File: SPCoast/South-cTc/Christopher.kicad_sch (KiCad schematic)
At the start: 23 parts, among them U28 0x27, U29 0x28, U30 0x29

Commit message: SPCoast: owner's edits: schematics synced with the revised symbol libraries (baseline)
Update Symbols from Library on all plant and desk sheets; CP values for
Christopher, GilroyInterchange and Luchessa; Restricted Speed markers
consolidated in Corporal, Luchessa and Sargent.

Observed in the diff, not changed by the sweep that follows: CP changed on 23
symbols (Christopher: prefix removed, 815/815A/IND now Christopher North) and
added on 12 (GilroyInterchange); two lamps' Color reset to their symbol variant
(Christopher LMP93 red -> yellow, Sargent LMP133 yellow -> red).

Verified: netlists keep their net counts (Christopher 33, Corporal 26,
GilroyCalTrain 27, GilroyInterchange 22, Luchessa 34, Sargent 18, Watsonville
96, South-cTc 341); desk compiles to 75 appliances, 137 bindings, 14 columns;
no root-UUID regression.

Co-Authored-By: Claude Sonnet 5.5 <noreply@anthropic.com>
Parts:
- LMP93: Color red -> yellow
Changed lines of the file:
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@@
 			)
 		)
-		(property "Description" "One physical desk lamp. Value is a free descriptive label (e.g. OS, TRACK, MC) and is not used elsewhere. IndicationToken is a comma-separated list of indication names (track circuits such as 795T1,2NAA,799T1, or tokens such as MC1K) OR'd to drive this one lamp. All listed indications are still individually on the CodeLine wire"
+		(property "Description" "One physical model board lamp. Value is a free descriptive label (e.g. OS, TRACK, MC) and is not used elsewhere. IndicationToken is a comma-separated list of indication names (track circuits such as 795T1,2NAA,799T1, or tokens such as MC1K) OR'd to drive this one lamp. All listed indications are still individually on the CodeLine wire"
 			(at 181.61 111.76 0)
 			(hide yes)
@@
 			)
 		)
-		(property "Description" "One physical desk lamp. Value is a free descriptive label (e.g. OS, TRACK, MC) and is not used elsewhere. IndicationToken is a comma-separated list of indication names (track circuits such as 795T1,2NAA,799T1, or tokens such as MC1K) OR'd to drive this one lamp. All listed indications are still individually on the CodeLine wire"
+		(property "Description" "One physical model board lamp. Value is a free descriptive label (e.g. OS, TRACK, MC) and is not used elsewhere. IndicationToken is a comma-separated list of indication names (track circuits such as 795T1,2NAA,799T1, or tokens such as MC1K) OR'd to drive this one lamp. All listed indications are still individually on the CodeLine wire"
 			(at 130.175 36.195 0)
 			(hide yes)
@@
 			)
 		)
-		(property "Description" "One physical desk lamp. Value is a free descriptive label (e.g. OS, TRACK, MC) and is not used elsewhere. IndicationToken is a comma-separated list of indication names (track circuits such as 795T1,2NAA,799T1, or tokens such as MC1K) OR'd to drive this one lamp. All listed indications are still individually on the CodeLine wire"
+		(property "Description" "One physical model board lamp. Value is a free descriptive label (e.g. OS, TRACK, MC) and is not used elsewhere. IndicationToken is a comma-separated list of indication names (track circuits such as 795T1,2NAA,799T1, or tokens such as MC1K) OR'd to drive this one lamp. All listed indications are still individually on the CodeLine wire"
 			(at 181.61 39.37 0)
 			(hide yes)
@@
 			)
 		)
-		(property "Description" "One physical desk lamp. Value is a free descriptive label (e.g. OS, TRACK, MC) and is not used elsewhere. IndicationToken is a comma-separated list of indication names (track circuits such as 795T1,2NAA,799T1, or tokens such as MC1K) OR'd to drive this one lamp. All listed indications are still individually on the CodeLine wire"
+		(property "Description" "One physical model board lamp. Value is a free descriptive label (e.g. OS, TRACK, MC) and is not used elsewhere. IndicationToken is a comma-separated list of indication names (track circuits such as 795T1,2NAA,799T1, or tokens such as MC1K) OR'd to drive this one lamp. All listed indications are still individually on the CodeLine wire"
 			(at 80.01 44.45 0)
 			(hide yes)
@@
 			)
 		)
-		(property "Description" "One physical desk lamp. Value is a free descriptive label (e.g. OS, TRACK, MC) and is not used elsewhere. IndicationToken is a comma-separated list of indication names (track circuits such as 795T1,2NAA,799T1, or tokens such as MC1K) OR'd to drive this one lamp. All listed indications are still individually on the CodeLine wire"
+		(property "Description" "One physical model board lamp. Value is a free descriptive label (e.g. OS, TRACK, MC) and is not used elsewhere. IndicationToken is a comma-separated list of indication names (track circuits such as 795T1,2NAA,799T1, or tokens such as MC1K) OR'd to drive this one lamp. All listed indications are still individually on the CodeLine wire"
 			(at 181.61 44.45 0)
 			(hide yes)
@@
 			)
 		)
-		(property "Color" "red"
+		(property "Color" "yellow"
 			(at 181.61 43.18 0)
 			(hide yes)
@@
 			)
 		)
-		(property "Description" "One physical desk lamp. Value is a free descriptive label (e.g. OS, TRACK, MC) and is not used elsewhere. IndicationToken is a comma-separated list of indication names (track circuits such as 795T1,2NAA,799T1, or tokens such as MC1K) OR'd to drive this one lamp. All listed indications are still individually on the CodeLine wire"
+		(property "Description" "One physical model board lamp. Value is a free descriptive label (e.g. OS, TRACK, MC) and is not used elsewhere. IndicationToken is a comma-separated list of indication names (track circuits such as 795T1,2NAA,799T1, or tokens such as MC1K) OR'd to drive this one lamp. All listed indications are still individually on the CodeLine wire"
 			(at 80.01 39.37 0)
 			(hide yes)
@@
 			)
 		)
-		(property "Description" "One physical desk lamp. Value is a free descriptive label (e.g. OS, TRACK, MC) and is not used elsewhere. IndicationToken is a comma-separated list of indication names (track circuits such as 795T1,2NAA,799T1, or tokens such as MC1K) OR'd to drive this one lamp. All listed indications are still individually on the CodeLine wire"
+		(property "Description" "One physical model board lamp. Value is a free descriptive label (e.g. OS, TRACK, MC) and is not used elsewhere. IndicationToken is a comma-separated list of indication names (track circuits such as 795T1,2NAA,799T1, or tokens such as MC1K) OR'd to drive this one lamp. All listed indications are still individually on the CodeLine wire"
 			(at 80.01 34.29 0)
 			(hide yes)
@@
 			)
 		)
-		(property "Description" "One physical desk lamp. Value is a free descriptive label (e.g. OS, TRACK, MC) and is not used elsewhere. IndicationToken is a comma-separated list of indication names (track circuits such as 795T1,2NAA,799T1, or tokens such as MC1K) OR'd to drive this one lamp. All listed indications are still individually on the CodeLine wire"
+		(property "Description" "One physical model board lamp. Value is a free descriptive label (e.g. OS, TRACK, MC) and is not used elsewhere. IndicationToken is a comma-separated list of indication names (track circuits such as 795T1,2NAA,799T1, or tokens such as MC1K) OR'd to drive this one lamp. All listed indications are still individually on the CodeLine wire"
 			(at 80.01 111.76 0)
 			(hide yes)
@@
 			)
 		)
-		(property "Description" "One physical desk lamp. Value is a free descriptive label (e.g. OS, TRACK, MC) and is not used elsewhere. IndicationToken is a comma-separated list of indication names (track circuits such as 795T1,2NAA,799T1, or tokens such as MC1K) OR'd to drive this one lamp. All listed indications are still individually on the CodeLine wire"
+		(property "Description" "One physical model board lamp. Value is a free descriptive label (e.g. OS, TRACK, MC) and is not used elsewhere. IndicationToken is a comma-separated list of indication names (track circuits such as 795T1,2NAA,799T1, or tokens such as MC1K) OR'd to drive this one lamp. All listed indications are still individually on the CodeLine wire"
 			(at 130.175 41.275 0)
 			(hide yes)
@@
 			)
 		)
-		(property "Description" "Generic 1-bit dispatcher-facing appliance (Maintainer Call, switch heater, bungalow door, etc).  ControlToken must be declared explicitly."
+		(property "Description" "Maintainer Call Lever"
 			(at 181.61 55.245 0)
 			(hide yes)
@@
 			)
 		)
-		(property "Description" "Generic 1-bit dispatcher-facing appliance (Maintainer Call, switch heater, bungalow door, etc).  ControlToken must be declared explicitly."
+		(property "Description" "Maintainer Call Lever"
 			(at 80.01 55.245 0)
 			(hide yes)
@@
 			)
 		)
-		(property "Description" "One physical desk lamp. Value is a free descriptive label (e.g. OS, TRACK, MC) and is not used elsewhere. IndicationToken is a comma-separated list of indication names (track circuits such as 795T1,2NAA,799T1, or tokens such as MC1K) OR'd to drive this one lamp. All listed indications are still individually on the CodeLine wire"
+		(property "Description" "One physical model board lamp. Value is a free descriptive label (e.g. OS, TRACK, MC) and is not used elsewhere. IndicationToken is a comma-separated list of indication names (track circuits such as 795T1,2NAA,799T1, or tokens such as MC1K) OR'd to drive this one lamp. All listed indications are still individually on the CodeLine wire"
 			(at 181.61 34.29 0)
 			(hide yes)

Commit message: SPCoast: owner's edits: Christopher OS lamps 813T1 and 817T1 use the red variant; Watsonville MAIN HOUSE LABEL removed (baseline)
Co-Authored-By: Claude Sonnet 5.5 <noreply@anthropic.com>
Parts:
- LMP82, LMP93: symbol RailroadPanel:PanelLamp-YELLOW -> RailroadPanel:PanelLamp-RED
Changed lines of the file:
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@@
 	)
 	(symbol
-		(lib_id "RailroadPanel:PanelLamp-YELLOW")
+		(lib_id "RailroadPanel:PanelLamp-RED")
 		(at 181.61 36.83 0)
 		(unit 1)
@@
 		)
 		(property "Color" "yellow"
-			(at 181.61 43.18 0)
+			(at 180.975 45.085 0)
 			(hide yes)
-			(show_name no)
+			(show_name yes)
 			(do_not_autoplace no)
 			(effects
@@
 	)
 	(symbol
-		(lib_id "RailroadPanel:PanelLamp-YELLOW")
+		(lib_id "RailroadPanel:PanelLamp-RED")
 		(at 80.01 31.75 0)
 		(unit 1)
@@
 		)
 		(property "Color" "yellow"
-			(at 80.01 38.1 0)
+			(at 79.375 40.005 0)
 			(hide yes)
-			(show_name no)
+			(show_name yes)
 			(do_not_autoplace no)
 			(effects

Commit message: fix(kicad): Christopher lamps 813T1 and 817T1: Color follows the red symbol variant
Change Symbol kept the old Color field (yellow) when the owner switched the two
OS lamps to PanelLamp-RED. Color is now red, so field and variant agree again.

Verified: all PanelLamp instances in South-cTc/Christopher now have Color equal
to their symbol variant; desk compiles to 75 appliances, 137 bindings, 14 columns.

Co-Authored-By: Claude Sonnet 5.5 <noreply@anthropic.com>
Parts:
- LMP82, LMP93: Color yellow -> red
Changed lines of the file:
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@@
 			)
 		)
-		(property "Color" "yellow"
+		(property "Color" "red"
 			(at 180.975 45.085 0)
 			(hide yes)
@@
 			)
 		)
-		(property "Color" "yellow"
+		(property "Color" "red"
 			(at 79.375 40.005 0)
 			(hide yes)

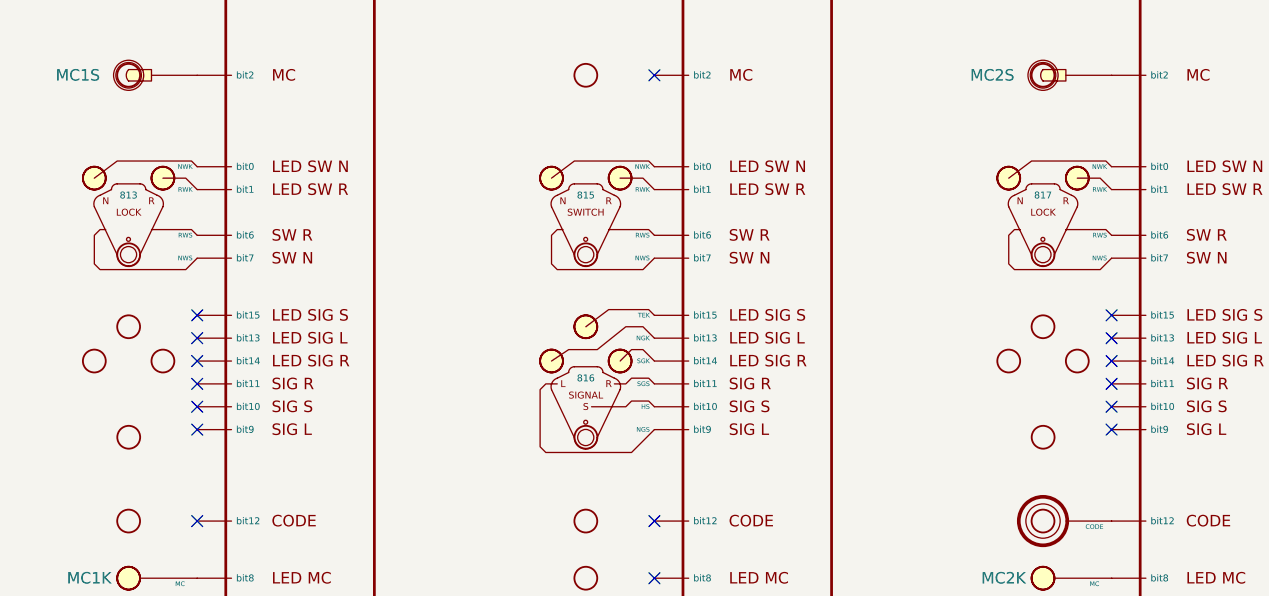
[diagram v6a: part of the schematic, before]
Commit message: chore(kicad): refresh instances to the ADR 0003 libraries (InterlockingPlant 95f53e2)
- Desk sheets (South-cTc/*) and the Sargent sandbox: embedded PanelSwitch, PanelLock,
  PanelSignal, PanelMCall, PanelCode, PanelLamp-*, PanelColumn-MAX7313 definitions refreshed
  from the library (refresh_embedded.py, checked against the pre-pass library: only Description
  text had drifted). Instance Role APPLIANCE -> PANEL (77).
- Plant sheets: powered-switch instance Kind SWITCH_POWERED -> SWITCH_REMOTE (21), matching the
  library (sweep_role_kind_fields.py).

Verified:
- verify_symbol_diff.py: same symbols, lib_ids and positions; only Role/Kind changed.
- Nets unchanged: Christopher 30, Corporal 27, GilroyCalTrain 28, GilroyInterchange 23,
  Luchessa 35, Sargent 61, Watsonville 99, South-cTc 341.
- parse_kicad_plant.py --format text identical before/after for all seven plants.
- Desk compile 75/137/14, diagnostics identical; the 7 desk locks bind WLS/~{WLS}/~{WLK}/WLK
  to the bits that were NWS/RWS/RWK/NWK.
- No sheet or project outside Luchessa carries the copied root UUID.

Co-Authored-By: Claude Opus 5.5 <noreply@anthropic.com>
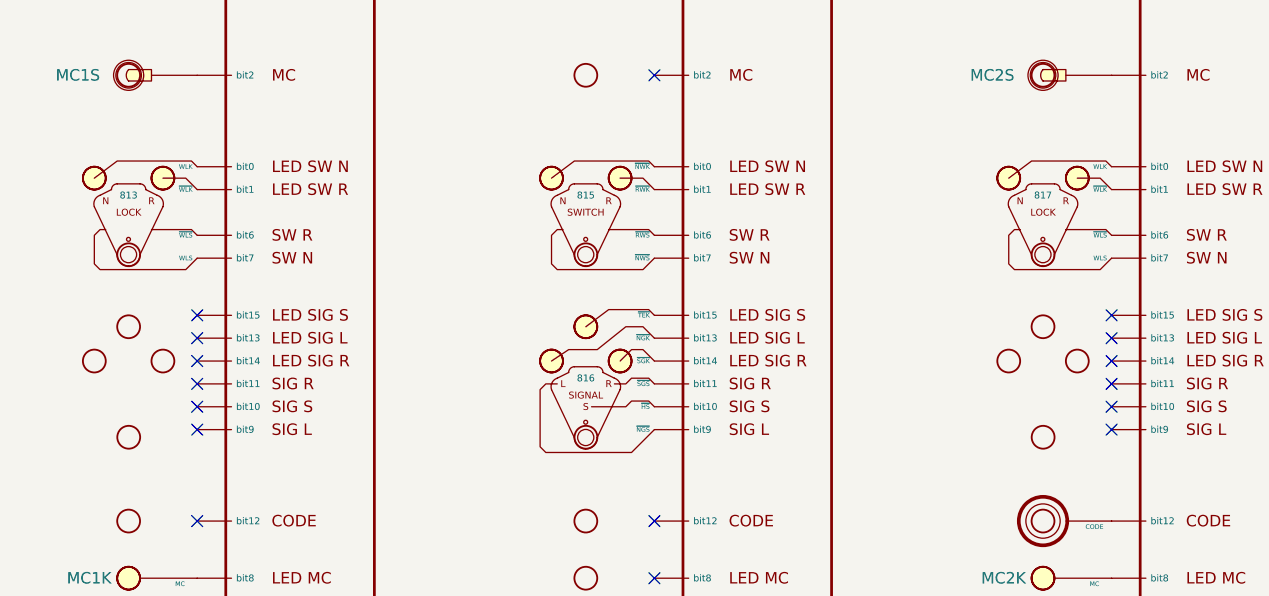
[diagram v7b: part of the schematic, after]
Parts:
- CDE10, LKL10, LKL8, LMP101, LMP102, LMP81, LMP82, LMP83, LMP91, LMP92, LMP93, MCK10, MCK8, MCL10, MCL8, SGL9, SWL9: Role APPLIANCE -> PANEL
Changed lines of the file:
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@@
 			)
 		)
-		(property "Role" "APPLIANCE"
+		(property "Role" "PANEL"
 			(at 130.81 92.71 0)
 			(hide yes)
@@
 			)
 		)
-		(property "Role" "APPLIANCE"
+		(property "Role" "PANEL"
 			(at 181.61 101.6 0)
 			(hide yes)
@@
 			)
 		)
-		(property "Role" "APPLIANCE"
+		(property "Role" "PANEL"
 			(at 130.81 29.21 0)
 			(hide yes)
@@
 			)
 		)
-		(property "Role" "APPLIANCE"
+		(property "Role" "PANEL"
 			(at 181.61 29.21 0)
 			(hide yes)
@@
 			)
 		)
-		(property "Role" "APPLIANCE"
+		(property "Role" "PANEL"
 			(at 80.01 34.29 0)
 			(hide yes)
@@
 			)
 		)
-		(property "Role" "APPLIANCE"
+		(property "Role" "PANEL"
 			(at 80.645 74.93 0)
 			(hide yes)
@@
 			)
 		)
-		(property "Role" "APPLIANCE"
+		(property "Role" "PANEL"
 			(at 181.61 34.29 0)
 			(hide yes)
@@
 			)
 		)
-		(property "Role" "APPLIANCE"
+		(property "Role" "PANEL"
 			(at 80.01 29.21 0)
 			(hide yes)
@@
 			)
 		)
-		(property "Role" "APPLIANCE"
+		(property "Role" "PANEL"
 			(at 80.01 24.13 0)
 			(hide yes)
@@
 			)
 		)
-		(property "Role" "APPLIANCE"
+		(property "Role" "PANEL"
 			(at 181.61 90.17 0)
 			(hide yes)
@@
 			)
 		)
-		(property "Role" "APPLIANCE"
+		(property "Role" "PANEL"
 			(at 182.245 74.93 0)
 			(hide yes)
@@
 			)
 		)
-		(property "Role" "APPLIANCE"
+		(property "Role" "PANEL"
 			(at 80.01 101.6 0)
 			(hide yes)
@@
 			)
 		)
-		(property "Role" "APPLIANCE"
+		(property "Role" "PANEL"
 			(at 131.445 76.2 0)
 			(hide yes)
@@
 			)
 		)
-		(property "Role" "APPLIANCE"
+		(property "Role" "PANEL"
 			(at 130.81 34.29 0)
 			(hide yes)
@@
 			)
 		)
-		(property "Role" "APPLIANCE"
+		(property "Role" "PANEL"
 			(at 187.96 44.45 0)
 			(hide yes)
@@
 			)
 		)
-		(property "Role" "APPLIANCE"
+		(property "Role" "PANEL"
 			(at 86.36 44.45 0)
 			(hide yes)
@@
 			)
 		)
-		(property "Role" "APPLIANCE"
+		(property "Role" "PANEL"
 			(at 181.61 24.13 0)
 			(hide yes)

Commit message: chore(kicad): desk sheets to Driver-I2C-MAX7313 and the PanelLock Kind (InterlockingPlant owner review)
- 14 desk expanders: lib_id RailroadPanel:PanelColumn-MAX7313 -> Driver-I2C-MAX7313, embedded
  definition refreshed (pins A1..B8, same numbers and positions).
- 8 PanelLock instances: Kind LOCK_LEVER -> LOCK_LEVER_2LAMP_2CONTACT (7 desk, 1 Sargent sandbox).

Verified:
- verify_symbol_diff.py: only those lib_id and Kind changes.
- South-cTc 341 nets, Sargent 61; desk compile 75/137/14 with bindings identical to e2c1093.

Co-Authored-By: Claude Opus 5.5 <noreply@anthropic.com>
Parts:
- LKL10, LKL8: Kind LOCK_LEVER -> LOCK_LEVER_2LAMP_2CONTACT
- U28, U29, U30: symbol RailroadPanel:PanelColumn-MAX7313 -> RailroadPanel:Driver-I2C-MAX7313
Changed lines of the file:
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@@
 	)
 	(symbol
-		(lib_id "RailroadPanel:PanelColumn-MAX7313")
+		(lib_id "RailroadPanel:Driver-I2C-MAX7313")
 		(at 149.86 72.39 0)
 		(unit 1)
@@
 	)
 	(symbol
-		(lib_id "RailroadPanel:PanelColumn-MAX7313")
+		(lib_id "RailroadPanel:Driver-I2C-MAX7313")
 		(at 200.66 72.39 0)
 		(unit 1)
@@
 			)
 		)
-		(property "Kind" "LOCK_LEVER"
+		(property "Kind" "LOCK_LEVER_2LAMP_2CONTACT"
 			(at 80.645 73.025 0)
 			(hide yes)
@@
 			)
 		)
-		(property "Kind" "LOCK_LEVER"
+		(property "Kind" "LOCK_LEVER_2LAMP_2CONTACT"
 			(at 182.245 73.025 0)
 			(hide yes)
@@
 	)
 	(symbol
-		(lib_id "RailroadPanel:PanelColumn-MAX7313")
+		(lib_id "RailroadPanel:Driver-I2C-MAX7313")
 		(at 99.06 72.39 0)
 		(unit 1)
